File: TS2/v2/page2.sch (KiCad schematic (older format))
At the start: 10 parts, among them J3 74LS148, J4 74LS138, J5 74LS138

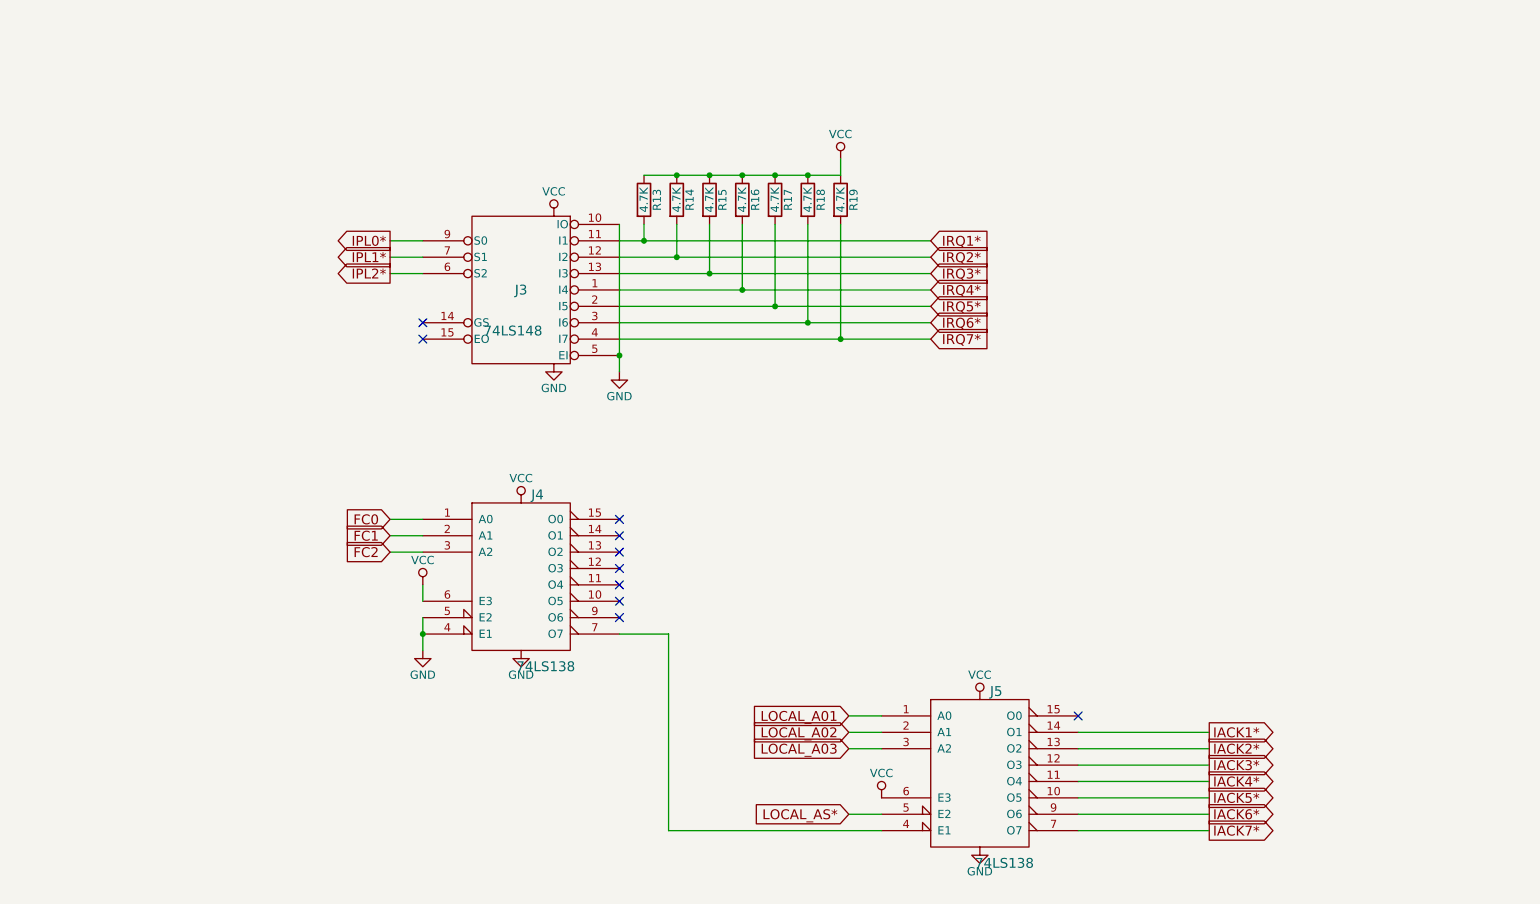
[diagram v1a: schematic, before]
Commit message: more fixup of deleted pages.
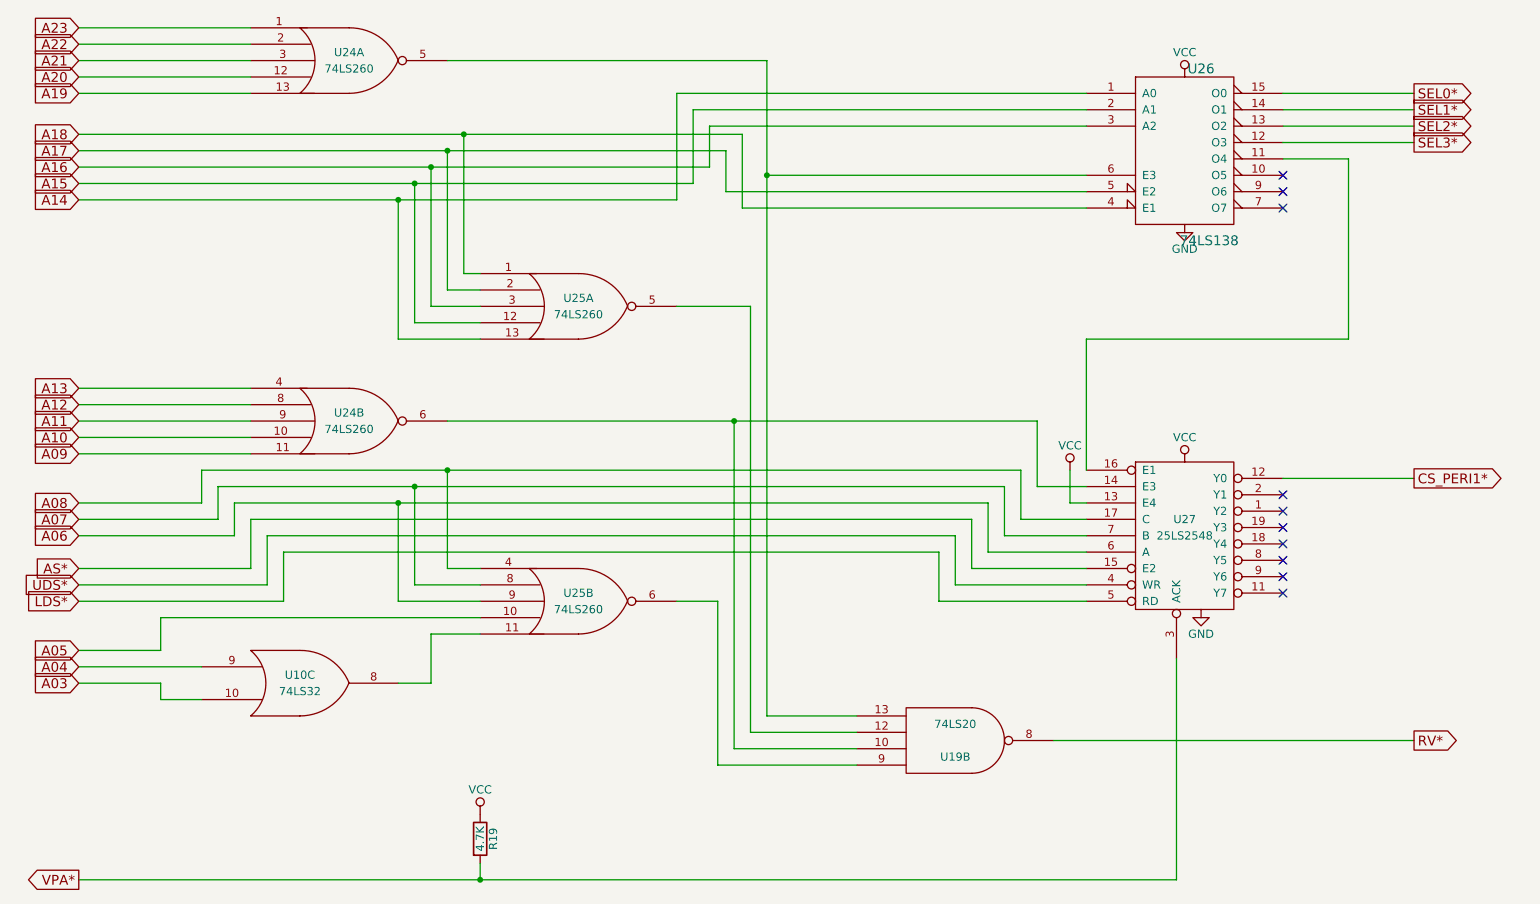
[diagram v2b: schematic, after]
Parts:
- removed J3: 74LS148, ~, symbol 74LS148
- removed J4, J5: 74LS138, ~, symbol 74LS138
- removed R13, R14, R15, R16, R17, R18: 4.7K, symbol R
- added U10: 74LS32, symbol 74LS32
- added U19: 74LS20, symbol 74LS20
- added U24, U25: 74LS260, symbol 74LS260
- added U26: 74LS138, ~, symbol 74LS138
- added U27: 25LS2548, symbol 25LS2548
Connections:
- net GND: now also U10.7 (GND), U19.7 (GND), U24.7 (GND), U24.7 (GND), U25.7 (GND), U25.7 (GND), U26.8 (GND), U27.10 (GND)
- net VCC: now also U10.14 (VCC), U19.14 (VCC), U24.14 (VCC), U24.14 (VCC), U25.14 (VCC), U25.14 (VCC), U26.16 (VCC), U27.13 (E4), U27.20 (VCC)
- net IRQ7* renamed VPA*
- net VPA*: now also U27.3 (ACK)
- new net: U26.11 (O4), U27.16 (E1)
- new net: U19.13, U24.5, U26.6 (E3)
- new net: U10.8, U25.11
- new net: U19.10, U24.6, U27.14 (E3)
- new net: U19.12, U25.5
- new net: U19.9, U25.6
- new net A03: U10.10
- new net A04: U10.9
- new net A05: U25.10
- new net A06: U25.9, U27.6 (A)
- new net A07: U25.8, U27.7 (B)
- new net A08: U25.4, U27.17 (C)
- new net A09: U24.11
- new net A10: U24.10
- new net A11: U24.9
- new net A12: U24.8
- new net A13: U24.4
- new net A14: U25.13, U26.1 (A0)
- new net A15: U25.12, U26.2 (A1)
- new net A16: U25.3, U26.3 (A2)
- new net A17: U25.2, U26.5 (E2)
- new net A18: U25.1, U26.4 (E1)
- new net A19: U24.13
- new net A20: U24.12
- new net A21: U24.3
- new net A22: U24.2
- new net A23: U24.1
- new net AS*: U27.15 (E2)
- new net CS_PERI1*: U27.12 (Y0)
- new net LDS*: U27.5 (RD)
- new net RV*: U19.8
- new net SEL0*: U26.15 (O0)
- new net SEL1*: U26.14 (O1)
- new net SEL2*: U26.13 (O2)
- new net SEL3*: U26.12 (O3)
- new net UDS*: U27.4 (WR)

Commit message: Remove two duplicated pullup resistors. Route some signals better.
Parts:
- removed R19: 4.7K, symbol R
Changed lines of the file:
@@
 Sheet 3 8
 Title "TS2 68000 Single Board Computer"
-Date "2016-09-03"
+Date "2016-11-27"
 Rev "2.0"
 Comp "Jeff Tranter"
@@
 VPA*
 Wire Wire Line
-	1150 6200 7850 6200
-Wire Wire Line
 	8500 1400 9300 1400
 Text GLabel 9300 1400 2    60   Output ~ 0
@@
 Wire Wire Line
 	7850 6200 7850 4850
-$Comp
-L R R19
-U 1 1 57C1D3CA
-P 3600 5950
-F 0 "R19" V 3680 5950 50  0000 C CNN
-F 1 "4.7K" V 3600 5950 50  0000 C CNN
-F 2 "" V 3530 5950 50  0000 C CNN
-F 3 "" H 3600 5950 50  0000 C CNN
-	1    3600 5950
-	1    0    0    -1
-$EndComp
-$Comp
-L VCC #PWR029
-U 1 1 57C1D3F9
-P 3600 5800
-F 0 "#PWR029" H 3600 5650 50  0001 C CNN
-F 1 "VCC" H 3600 5950 50  0000 C CNN
-F 2 "" H 3600 5800 50  0000 C CNN
-F 3 "" H 3600 5800 50  0000 C CNN
-	1    3600 5800
-	1    0    0    -1
-$EndComp
-Wire Wire Line
-	3600 6100 3600 6200
-Connection ~ 3600 6200
 Wire Wire Line
 	7100 5350 9300 5350
@@
 	7200 3900 7200 3700
 $Comp
-L VCC #PWR030
+L VCC #PWR029
 U 1 1 57C1EB1C
 P 7200 3700
-F 0 "#PWR030" H 7200 3550 50  0001 C CNN
+F 0 "#PWR029" H 7200 3550 50  0001 C CNN
 F 1 "VCC" H 7200 3850 50  0000 C CNN
 F 2 "" H 7200 3700 50  0000 C CNN
@@
 NoConn ~ 8500 3850
 NoConn ~ 8500 3950
+Wire Wire Line
+	7850 6200 1150 6200
 $EndSCHEMATC
